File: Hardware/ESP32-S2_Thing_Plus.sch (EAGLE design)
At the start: 56 parts, among them J3 QWIIC_RA, J5 USB-C, J6 JTAG, Q1 2.5A/30V, Q2 MBT3904DW1T1, U1 MCP73831, U2 ESP32-S2-WROOM, U3 AP2112K-3.3V, U4 CP210X, Y1 32.768kHz

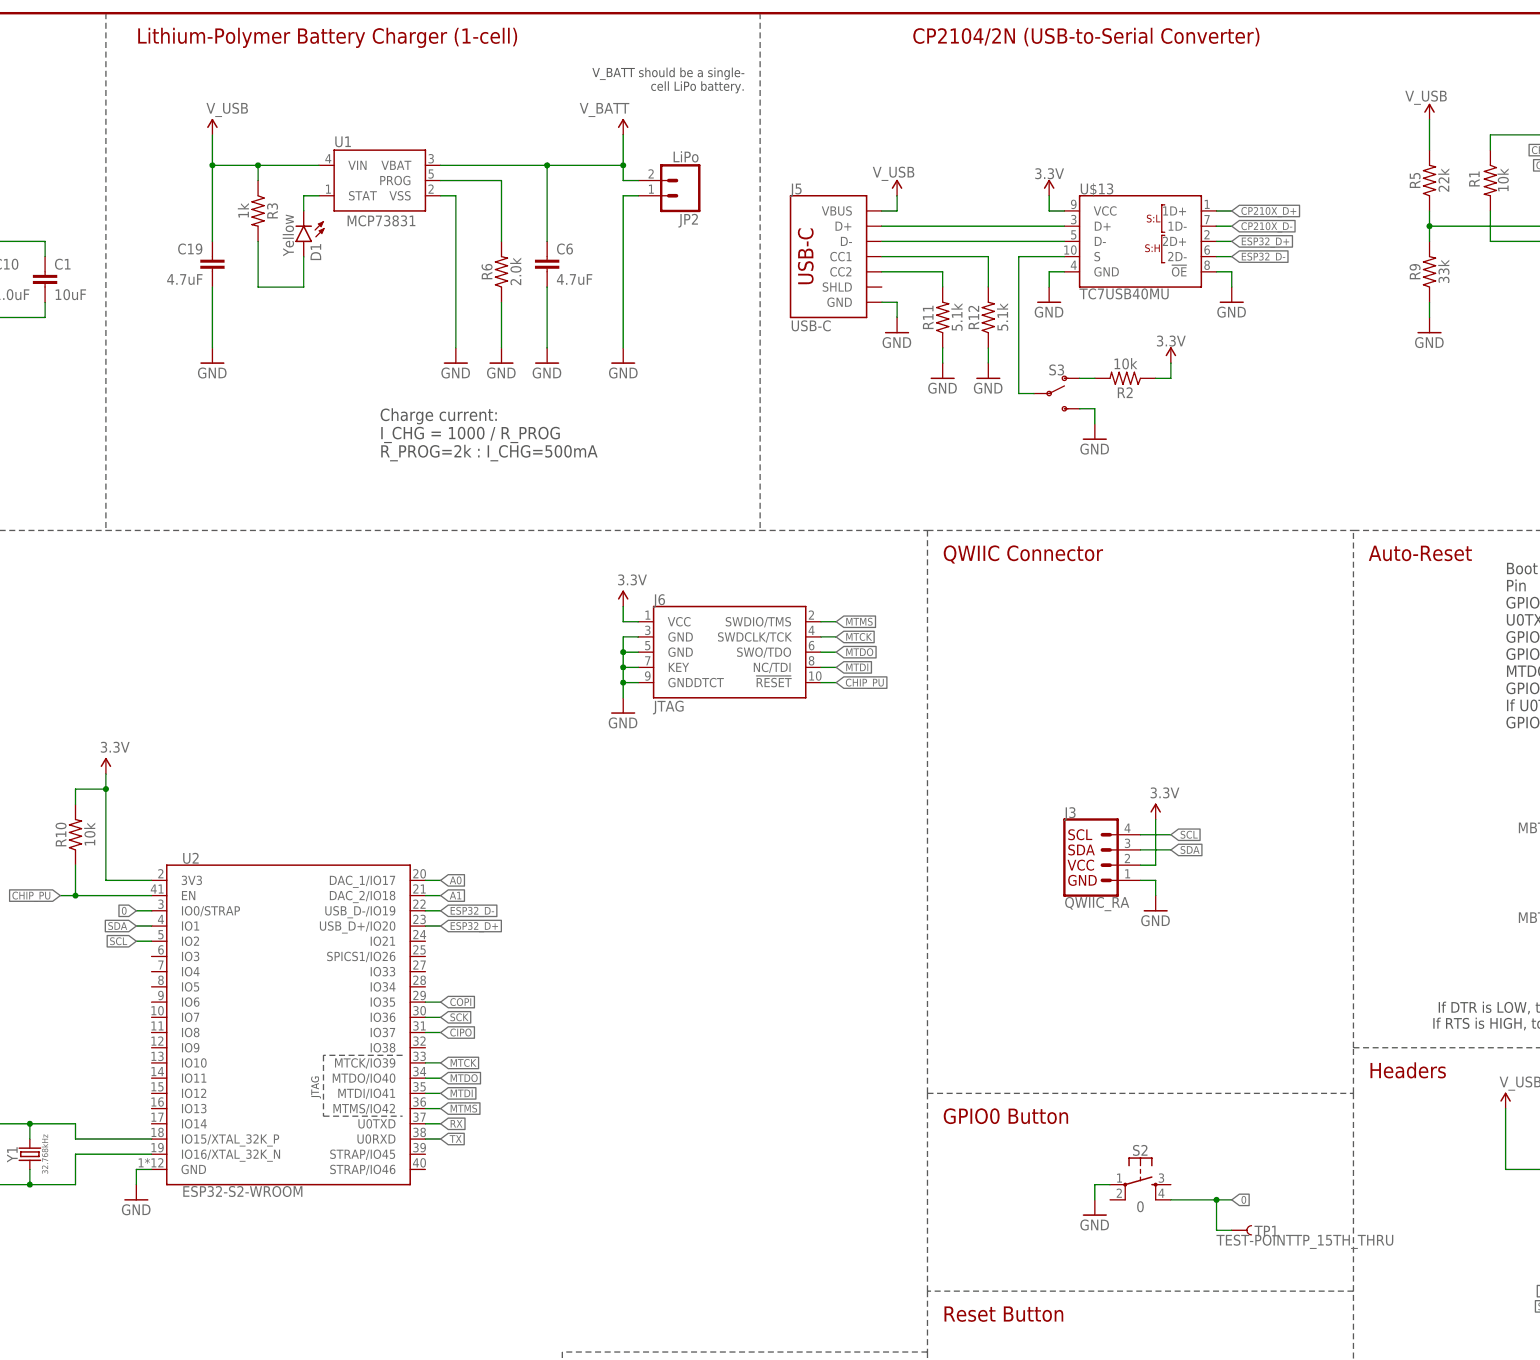
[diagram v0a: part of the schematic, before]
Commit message: added charge current jumper options and did a bunch of routing
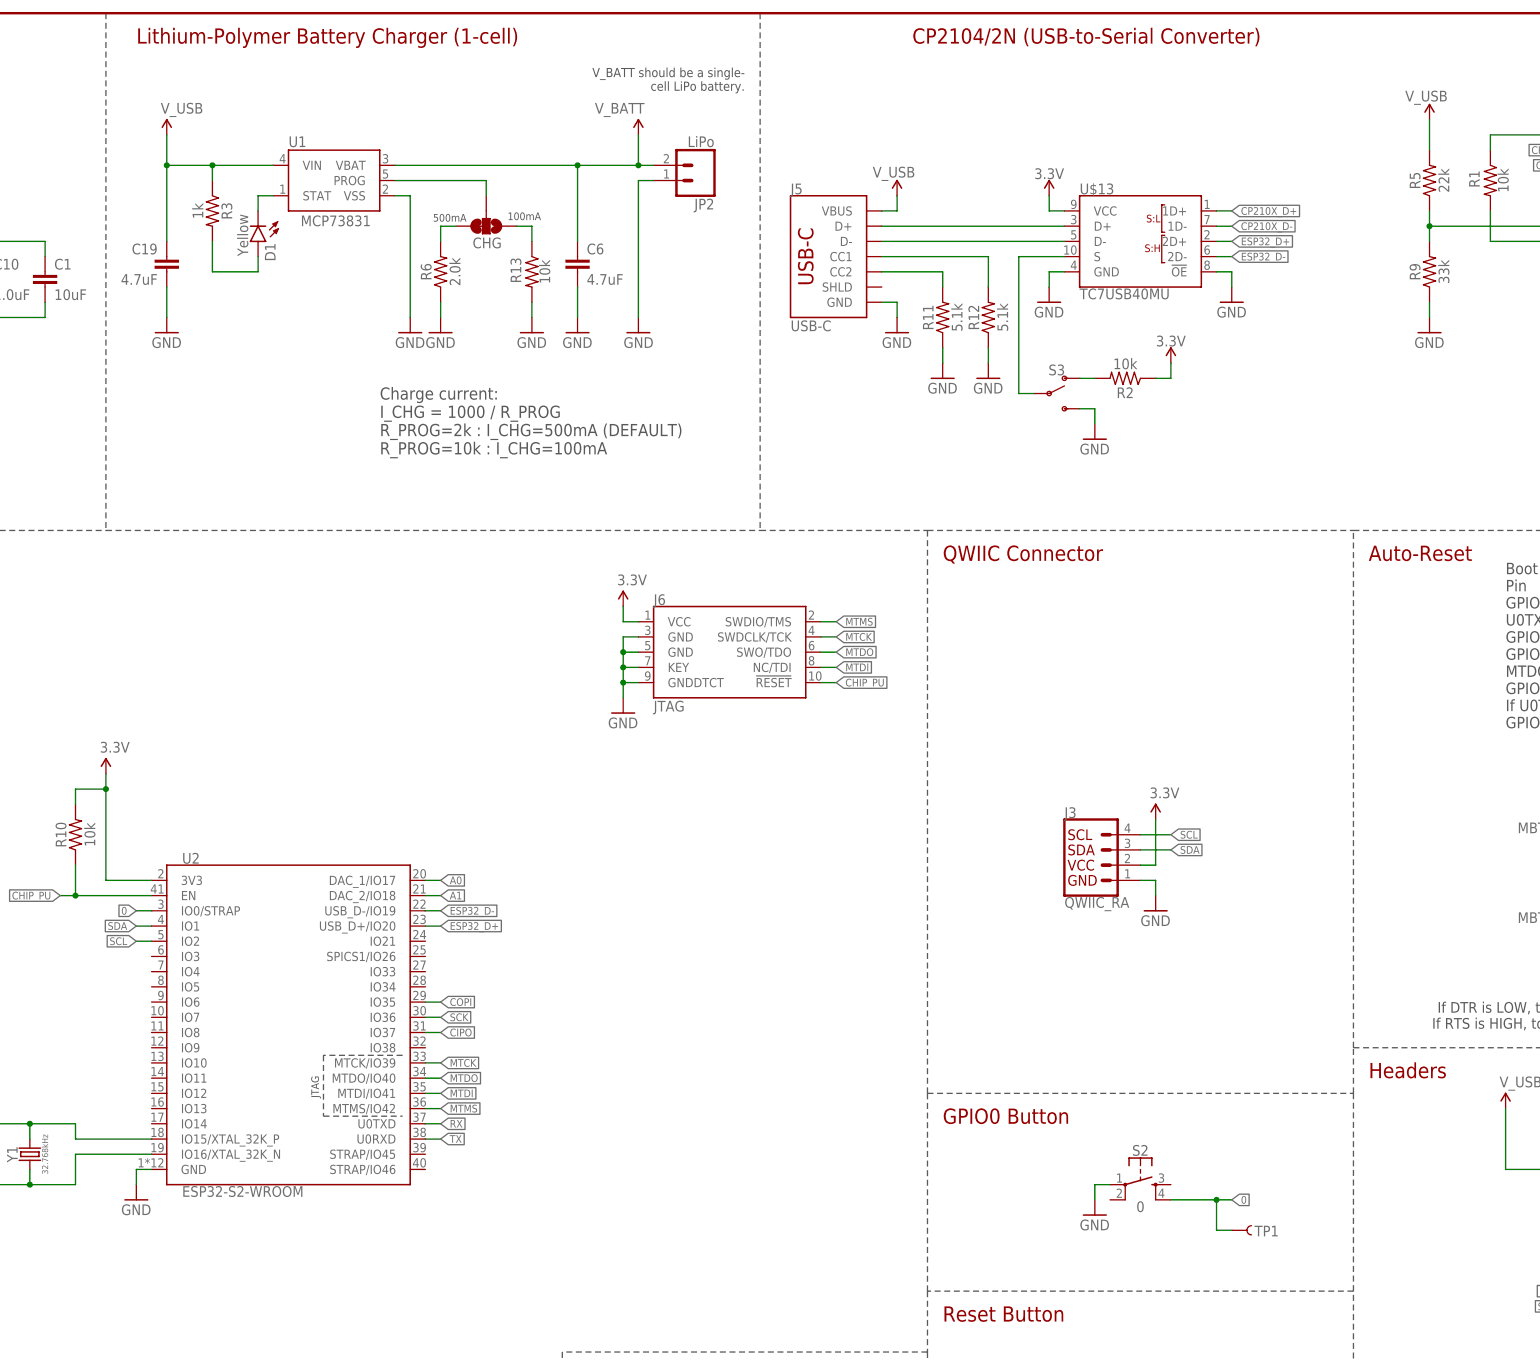
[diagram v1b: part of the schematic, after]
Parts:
- added CHG: JUMPER-SMT_3_1-NC_TRACE_SILK, SparkFun-Jumpers:JUMPER-SMT_3_1-NC_TRACE_SILK
- added R13: 10k, SparkFun-Resistors:10KOHM-0402T-1/16W-1%
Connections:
- removed net N$14: R6.2, U1.PROG
- new net N$11: CHG.1, R13.1
- new net N$13: CHG.3, R6.2
- new net N$9: CHG.2, U1.PROG
- net GND: now also R13.2
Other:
- note added: "100mA"
- note added: "500mA"
- note added: "Charge current: I_CHG = 1000 / R_PROG R_PROG=2k : I_CHG=500mA (DEFAULT) R_PROG=10k : I_CHG=100mA"
- note removed: "Charge current: I_CHG = 1000 / R_PROG R_PROG=2k : I_CHG=500mA"
- moved on the sheet: C19, C6, D1, JP2, R3, R6, U1

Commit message: Moved to smaller/newer 32.768kHz crystal
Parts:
- C4, C5: value 22pF -> 15pF; device SparkFun-Capacitors:22PF-0402T-16V-10% -> SparkFun-Capacitors:15PF-0402T-50V-5%
- Y1: device SparkFun-Clocks:CRYSTAL-32.768KHZSMD-2X6 -> SparkFun-Clocks:CRYSTAL-32.768KHZSMD-3.2X1.5
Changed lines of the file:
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@@
 <part name="SUPPLY13" library="SparkFun-Aesthetics" deviceset="3.3V" device=""/>
 <part name="S3" library="SparkFun-Switches" deviceset="SWITCH-SPDT" device="-SMD-RIGHT-ANGLE"/>
-<part name="Y1" library="SparkFun-Clocks" deviceset="CRYSTAL-32.768KHZ" device="SMD-2X6" value="32.768kHz"/>
+<part name="Y1" library="SparkFun-Clocks" deviceset="CRYSTAL-32.768KHZ" device="SMD-3.2X1.5" value="32.768kHz"/>
 <part name="U$13" library="esp32-s2-wroom" deviceset="TC7USB40MU" device=""/>
 <part name="SUPPLY6" library="SparkFun-Aesthetics" deviceset="V_USB" device=""/>
@@
 <part name="SUPPLY15" library="SparkFun-PowerSymbols" deviceset="3.3V" device=""/>
 <part name="R2" library="SparkFun-Resistors" deviceset="10KOHM" device="-0402T-1/16W-1%" value="10k"/>
-<part name="C4" library="SparkFun-Capacitors" deviceset="22PF" device="-0402T-16V-10%" value="22pF"/>
-<part name="C5" library="SparkFun-Capacitors" deviceset="22PF" device="-0402T-16V-10%" value="22pF"/>
+<part name="C4" library="SparkFun-Capacitors" deviceset="15PF" device="-0402T-50V-5%" value="15pF"/>
+<part name="C5" library="SparkFun-Capacitors" deviceset="15PF" device="-0402T-50V-5%" value="15pF"/>
 <part name="GND23" library="SparkFun-Aesthetics" deviceset="GND" device=""/>
 <part name="R11" library="SparkFun-Resistors" deviceset="5.1KOHM" device="5.1KOHM-0603-1/10W-1%" value="5.1k"/>

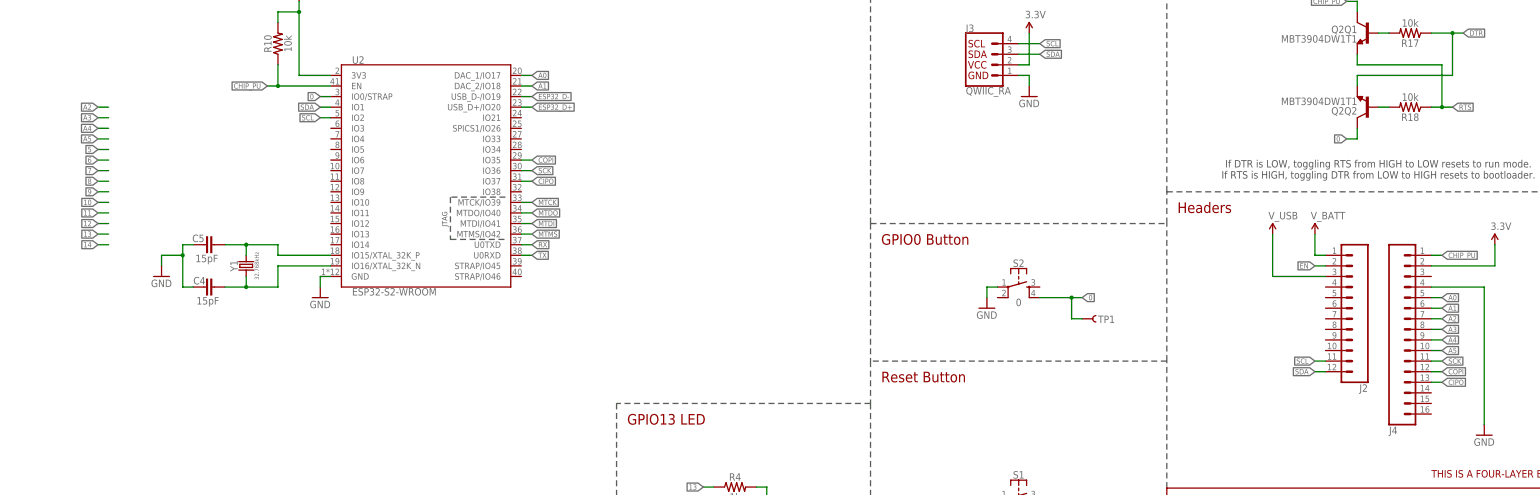
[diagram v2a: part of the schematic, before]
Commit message: All IO (except "extra SMD IO") routed
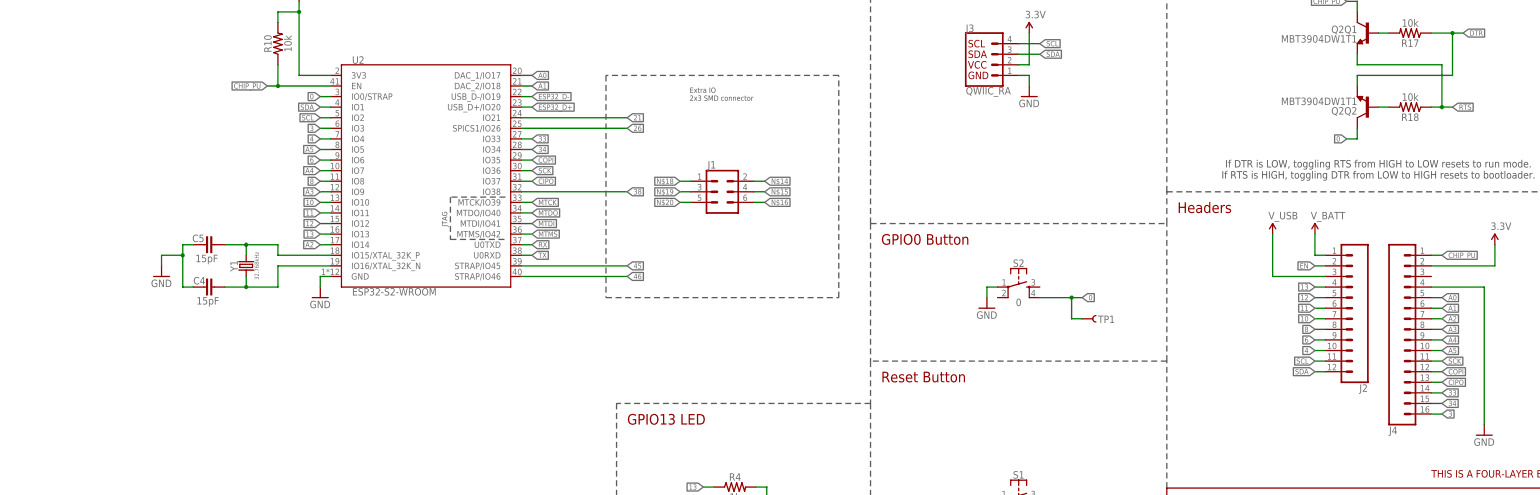
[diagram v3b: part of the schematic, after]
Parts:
- added J1: (no value), SparkFun-Connectors:CONN_03X2SMT
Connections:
- new net 10: J2.7, U2.IO10
- new net 11: J2.6, U2.IO11
- new net 12: J2.5, U2.IO12
- new net 21: U2.IO21
- new net 26: U2.SPICS1/IO26
- new net 3: J4.16, U2.IO3
- new net 33: J4.14, U2.IO33
- new net 34: J4.15, U2.IO34
- new net 38: U2.IO38
- new net 4: J2.10, U2.IO4
- new net 45: U2.STRAP/IO45
- new net 46: U2.STRAP/IO46
- new net 6: J2.9, U2.IO6
- new net 8: J2.8, U2.IO8
- new net N$14: J1.2
- new net N$15: J1.4
- new net N$16: J1.6
- new net N$18: J1.1
- new net N$19: J1.3
- new net N$20: J1.5
- net 13: now also J2.4, U2.IO13
- net A2: now also U2.IO14
- net A3: now also U2.IO9
- net A4: now also U2.IO7
- net A5: now also U2.IO5
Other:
- note added: "Extra IO 2x3 SMD connector"

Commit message: routing "done"
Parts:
- removed J1: (no value), SparkFun-Connectors:CONN_03X2SMT
- removed LOGO5: SFE_LOGO_NAME_FLAME.1_INCH, SparkFun-Aesthetics:SFE_LOGO_NAME_FLAME.1_INCH
- added J7: (no value), SparkFun-Connectors:CONN_04X2_SMT_NO_POSTS_NS
- added LOGO1: SFE_LOGO_FLAME.1_INCH, SparkFun-Aesthetics:SFE_LOGO_FLAME.1_INCH
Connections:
- net 33 renamed 33/RX1
- net 34 renamed 34/TX1
- removed net MTDI: J6.NC/TDI, U2.MTDI/IO41
- removed net N$14: J1.2
- removed net N$15: J1.4
- removed net N$16: J1.6
- removed net N$18: J1.1
- removed net N$19: J1.3
- removed net N$20: J1.5
- removed net RX: U2.U0TXD, U4.RXD
- removed net TX: U2.U0RXD, U4.TXD
- new net 41/MTDI: J6.NC/TDI, J7.7, U2.MTDI/IO41
- new net RX0: J7.5, U2.U0RXD, U4.TXD
- new net TX0: J7.6, U2.U0TXD, U4.RXD
- net 21: now also J7.2
- net 26: now also J7.4
- net 38: now also J7.8
- net 45: now also J7.3
- net 46: now also J7.1
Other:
- note added: "JTAG"
- moved on the sheet: C4, C5, J6, R10, U2, Y1

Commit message: schematic cleanup and added recommended RC (cap to GND) on enable pin
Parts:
- removed U$13: TC7USB40MU, esp32-s2-wroom:TC7USB40MU
- added C8: 0.1uF, SparkFun-Capacitors:0.1UF-0402T-16V-10%
- added U5: TC7USB40MU, esp32-s2-wroom:TC7USB40MU
- U1: value MCP73831 -> ESP32-S2-WROOM; device SparkFun-PowerIC:MCP73831 -> esp32-s2-wroom:ESP32-S2-WROOM
- U2: value ESP32-S2-WROOM -> CP210X; device esp32-s2-wroom:ESP32-S2-WROOM -> SparkFun-IC-Comms:CP2102N
- U4: value CP210X -> MCP73831; device SparkFun-IC-Comms:CP2102N -> SparkFun-PowerIC:MCP73831
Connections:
- net 0: now also U1.IO0/STRAP; no longer U2.IO0/STRAP
- net 10: now also U1.IO10; no longer U2.IO10
- net 11: now also U1.IO11; no longer U2.IO11
- net 12: now also U1.IO12; no longer U2.IO12
- net 13: now also U1.IO13; no longer U2.IO13
- net 21: now also U1.IO21; no longer U2.IO21
- net 26: now also U1.SPICS1/IO26; no longer U2.SPICS1/IO26
- net 3: now also U1.IO3; no longer U2.IO3
- net 3.3V: now also U1.3V3, U2.VDD, U2.VIO, U2.VREGIN, U5.VCC; no longer U$13.VCC, U2.3V3, U4.VDD, U4.VIO, U4.VREGIN
- net 33/RX1: now also U1.IO33; no longer U2.IO33
- net 34/TX1: now also U1.IO34; no longer U2.IO34
- net 38: now also U1.IO38; no longer U2.IO38
- net 4: now also U1.IO4; no longer U2.IO4
- net 41/MTDI: now also U1.MTDI/IO41; no longer U2.MTDI/IO41
- net 45: now also U1.STRAP/IO45; no longer U2.STRAP/IO45
- net 46: now also U1.STRAP/IO46; no longer U2.STRAP/IO46
- net 6: now also U1.IO6; no longer U2.IO6
- net 8: now also U1.IO8; no longer U2.IO8
- net A0: now also U1.DAC_1/IO17; no longer U2.DAC_1/IO17
- net A1: now also U1.DAC_2/IO18; no longer U2.DAC_2/IO18
- net A2: now also U1.IO14; no longer U2.IO14
- net A3: now also U1.IO9; no longer U2.IO9
- net A4: now also U1.IO7; no longer U2.IO7
- net A5: now also U1.IO5; no longer U2.IO5
- net CHG: now also U4.STAT; no longer U1.STAT
- net CHIP_PU: now also C8.1, U1.EN; no longer U2.EN
- net CIPO: now also U1.IO37; no longer U2.IO37
- net COPI: now also U1.IO35; no longer U2.IO35
- net CP210X_D+: now also U2.D+, U5.1D+; no longer U$13.1D+, U4.D+
- net CP210X_D-: now also U2.D-, U5.1D-; no longer U$13.1D-, U4.D-
- net DTR: now also U2.DTR; no longer U4.DTR
- net ESP32_D+: now also U1.USB_D+/IO20, U5.2D+; no longer U$13.2D+, U2.USB_D+/IO20
- net ESP32_D-: now also U1.USB_D-/IO19, U5.2D-; no longer U$13.2D-, U2.USB_D-/IO19
- net GND: now also C8.2, U1.GND, U4.VSS, U5.!OE!, U5.GND; no longer U$13.!OE!, U$13.GND, U1.VSS, U4.GND
- net MTCK: now also U1.MTCK/IO39; no longer U2.MTCK/IO39
- net MTDO: now also U1.MTDO/IO40; no longer U2.MTDO/IO40
- net MTMS: now also U1.MTMS/IO42; no longer U2.MTMS/IO42
- net N$1: now also U2.!RSTB; no longer U4.!RSTB
- net N$3: now also U5.D+; no longer U$13.D+
- net N$4: now also U2.VBUS; no longer U4.VBUS
- net N$5: now also U5.D-; no longer U$13.D-
- net N$7: now also U1.IO15/XTAL_32K_P; no longer U2.IO15/XTAL_32K_P
- net N$8: now also U1.IO16/XTAL_32K_N; no longer U2.IO16/XTAL_32K_N
- net N$9: now also U4.PROG; no longer U1.PROG
- net RTS: now also U2.RTS; no longer U4.RTS
- net RX0: now also U1.U0RXD, U2.TXD; no longer U2.U0RXD, U4.TXD
- net SCK: now also U1.IO36; no longer U2.IO36
- net SCL: now also U1.IO2; no longer U2.IO2
- net SDA: now also U1.IO1; no longer U2.IO1
- net TX0: now also U1.U0TXD, U2.RXD; no longer U2.U0TXD, U4.RXD
- net USB_SEL: now also U5.S; no longer U$13.S
- net V_BATT: now also U4.VBAT; no longer U1.VBAT
- net V_USB: now also U4.VIN; no longer U1.VIN
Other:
- note added: "Module recommended VCC range: 3.0-3.6V"
- moved on the sheet: C1, C10, C19, C6, C7, CHG, D1, D2, J3, J5, JP2, Q1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

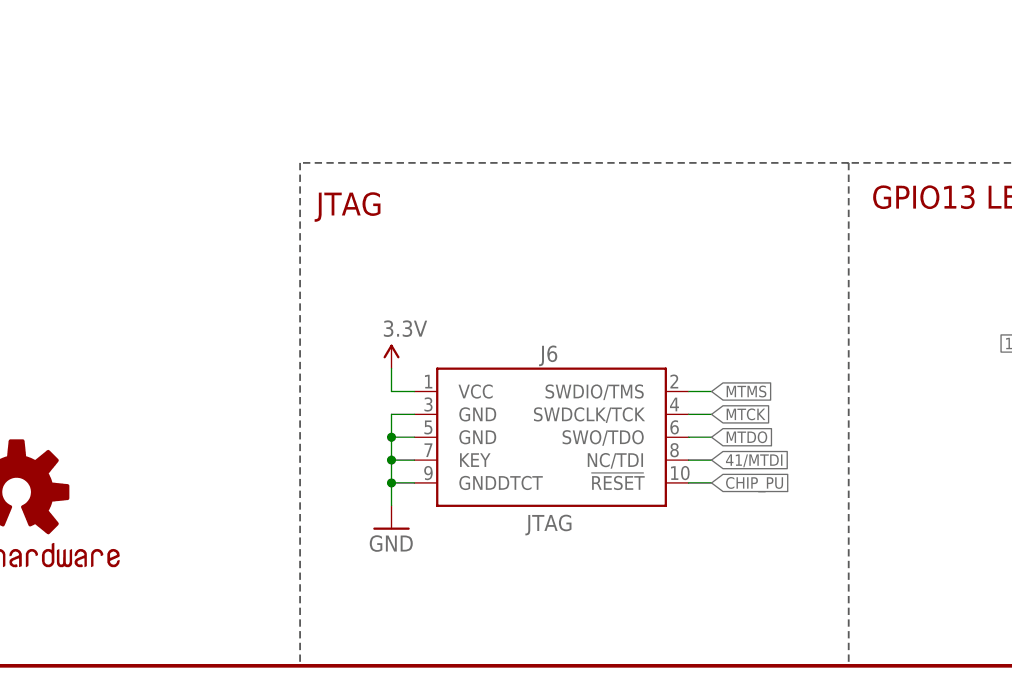
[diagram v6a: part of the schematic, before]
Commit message: added JTAG test points
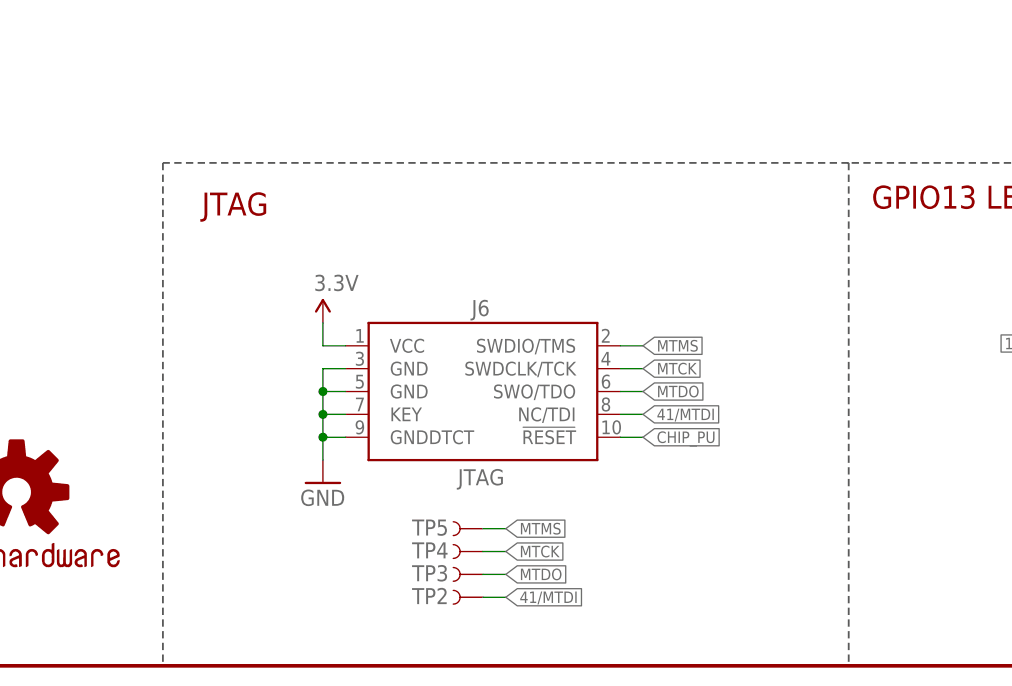
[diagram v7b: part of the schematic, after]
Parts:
- added TP2, TP3, TP4, TP5: TEST-POINT3X4, SparkFun-Connectors:TEST-POINT3X4
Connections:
- net 41/MTDI: now also TP2.1
- net MTCK: now also TP4.1
- net MTDO: now also TP3.1
- net MTMS: now also TP5.1
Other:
- moved on the sheet: J6
